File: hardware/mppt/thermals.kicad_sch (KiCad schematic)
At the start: 6 parts, among them M401 Fan

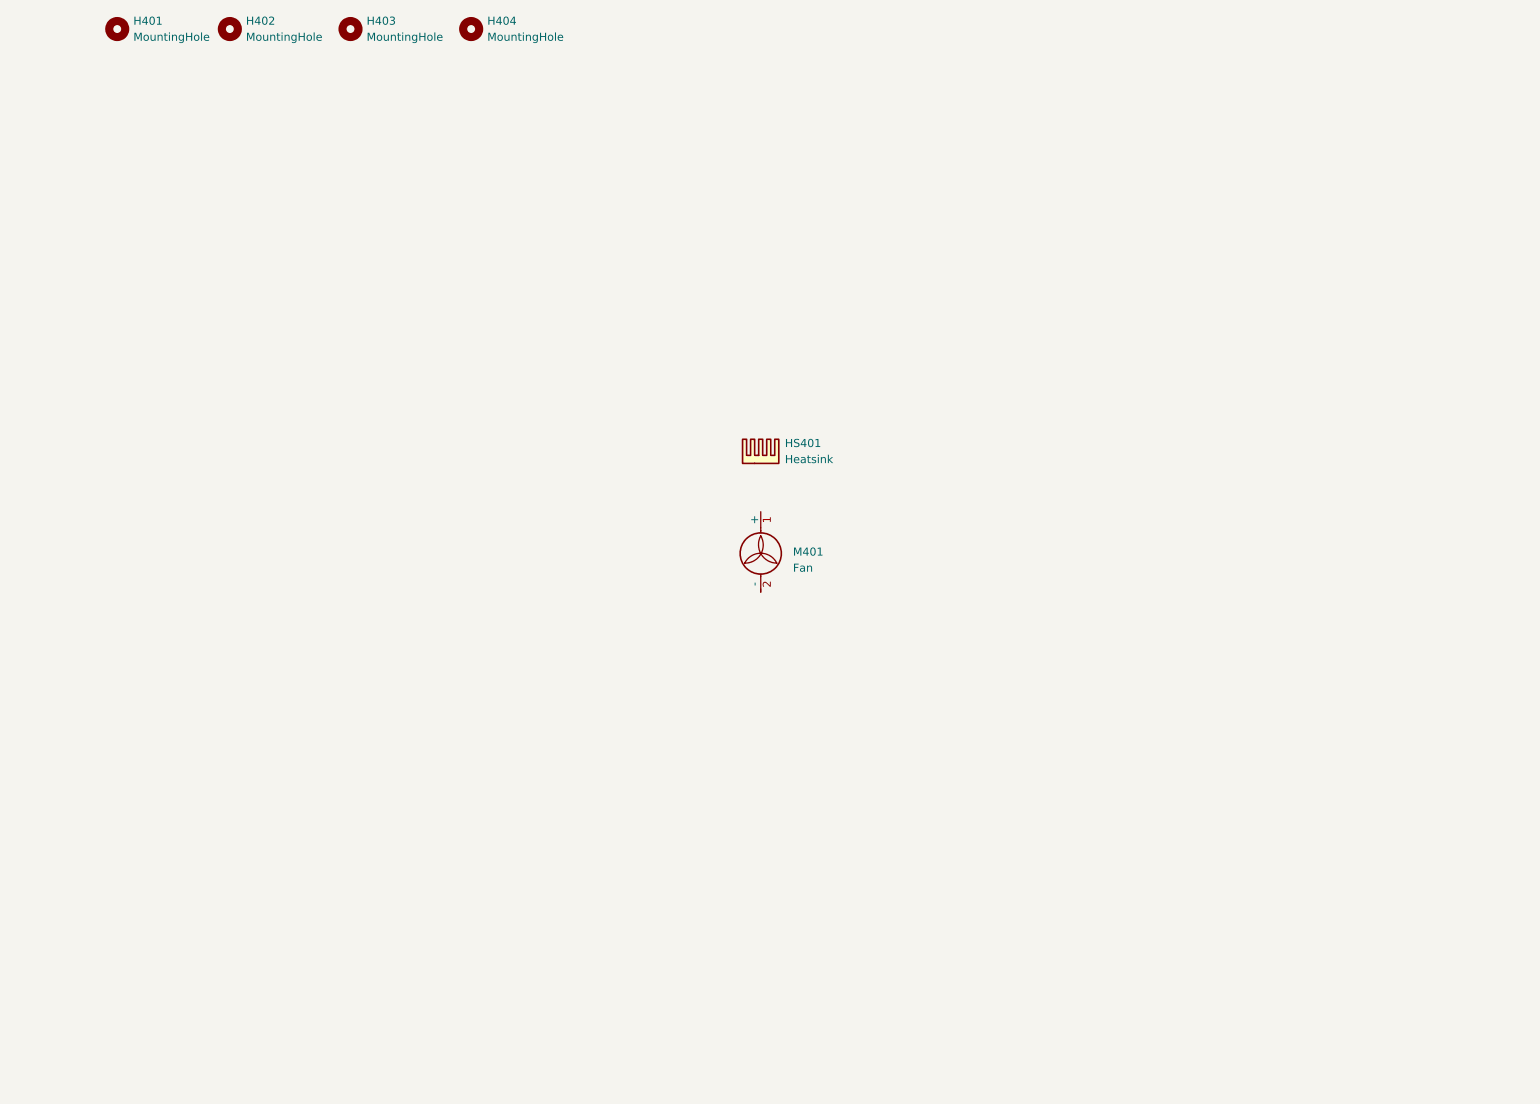
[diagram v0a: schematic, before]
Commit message: run through mppt sch, going through bom
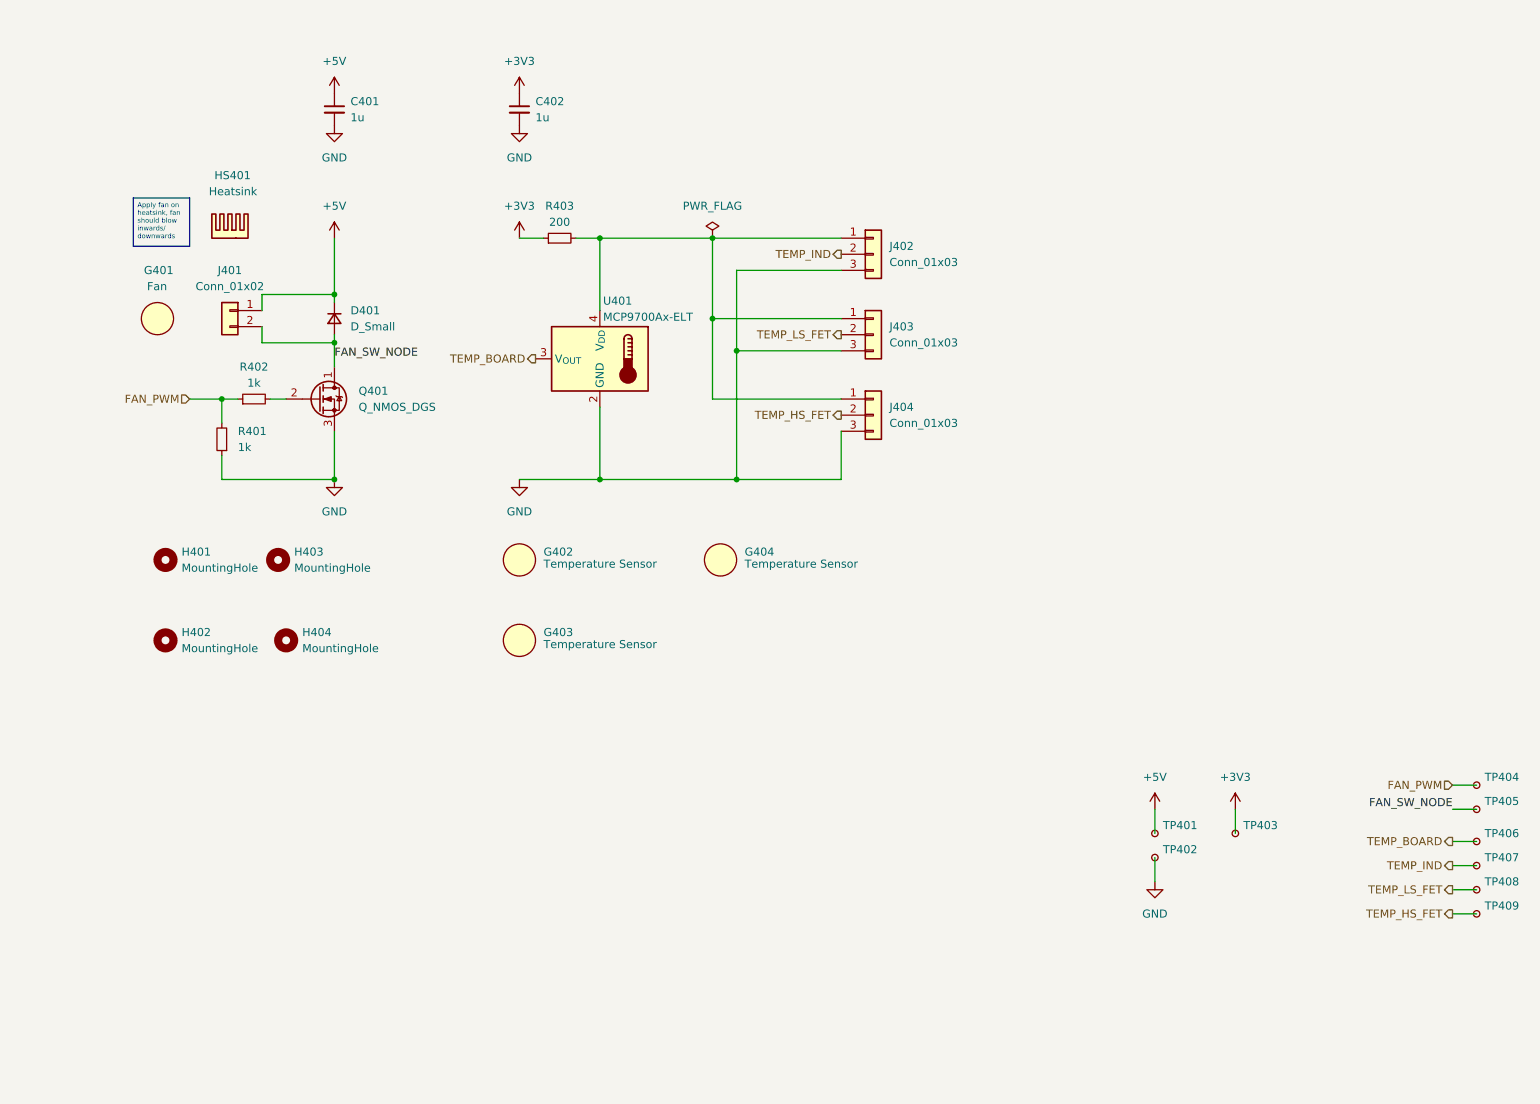
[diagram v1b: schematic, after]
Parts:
- removed M401: Fan, symbol Motor:Fan
- added C401, C402: 1u, symbol Device:C_Small
- added D401: D_Small, symbol Device:D_Small
- added G401: Fan, symbol generic_symbol:Generic_Symbol
- added G402, G403, G404: Temperature Sensor, symbol generic_symbol:Generic_Symbol
- added J401: Conn_01x02, symbol Connector_Generic:Conn_01x02
- added J402, J403, J404: Conn_01x03, symbol Connector_Generic:Conn_01x03
- added Q401: Q_NMOS_DGS, symbol Device:Q_NMOS_DGS
- added R401, R402: 1k, symbol Device:R_Small
- added R403: 200, symbol Device:R_Small
- added TP401, TP402, TP403, TP404, TP405, TP406, TP407, TP408, TP409: TestPoint_Small, TestPoint:TestPoint_Pad_D1.0mm, symbol Connector:TestPoint_Small
- added U401: MCP9700Ax-ELT, Package_TO_SOT_SMD:SOT-353_SC-70-5, symbol Sensor_Temperature:MCP9700Ax-ELT
- H401, H404: footprint MountingHole:MountingHole_5.3mm_M5 -> MountingHole:MountingHole_2.7mm_M2.5; Notes (none) -> M2.5 Hole
- H402: renamed from H403; footprint MountingHole:MountingHole_5.3mm_M5 -> MountingHole:MountingHole_2.7mm_M2.5; Notes (none) -> M2.5 Hole
- H403: renamed from H402; footprint MountingHole:MountingHole_5.3mm_M5 -> MountingHole:MountingHole_2.7mm_M2.5; Notes (none) -> M2.5 Hole
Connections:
- new net: J402.1 (Pin_1), J403.1 (Pin_1), J404.1 (Pin_1), R403.2, U401.4 (V_{DD})
- new net: Q401.2 (G), R402.2
- new net +3V3: C402.1, R403.1, TP403.1
- new net +5V: C401.1, D401.1 (K), J401.1 (Pin_1), TP401.1
- new net FAN_PWM: R401.2, R402.1, TP404.1
- new net FAN_SW_NODE: D401.2 (A), J401.2 (Pin_2), Q401.1 (D), TP405.1
- new net GND: C401.2, C402.2, J402.3 (Pin_3), J403.3 (Pin_3), J404.3 (Pin_3), Q401.3 (S), R401.1, TP402.1, U401.2 (GND)
- new net TEMP_BOARD: TP406.1, U401.3 (V_{OUT})
- new net TEMP_HS_FET: J404.2 (Pin_2), TP409.1
- new net TEMP_IND: J402.2 (Pin_2), TP407.1
- new net TEMP_LS_FET: J403.2 (Pin_2), TP408.1
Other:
- title: Mighty MPPT -> Thermals
- moved on the sheet: H401, H402, H403, H404, HS401

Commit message: update final missing pieces for sch, moving to bom pop
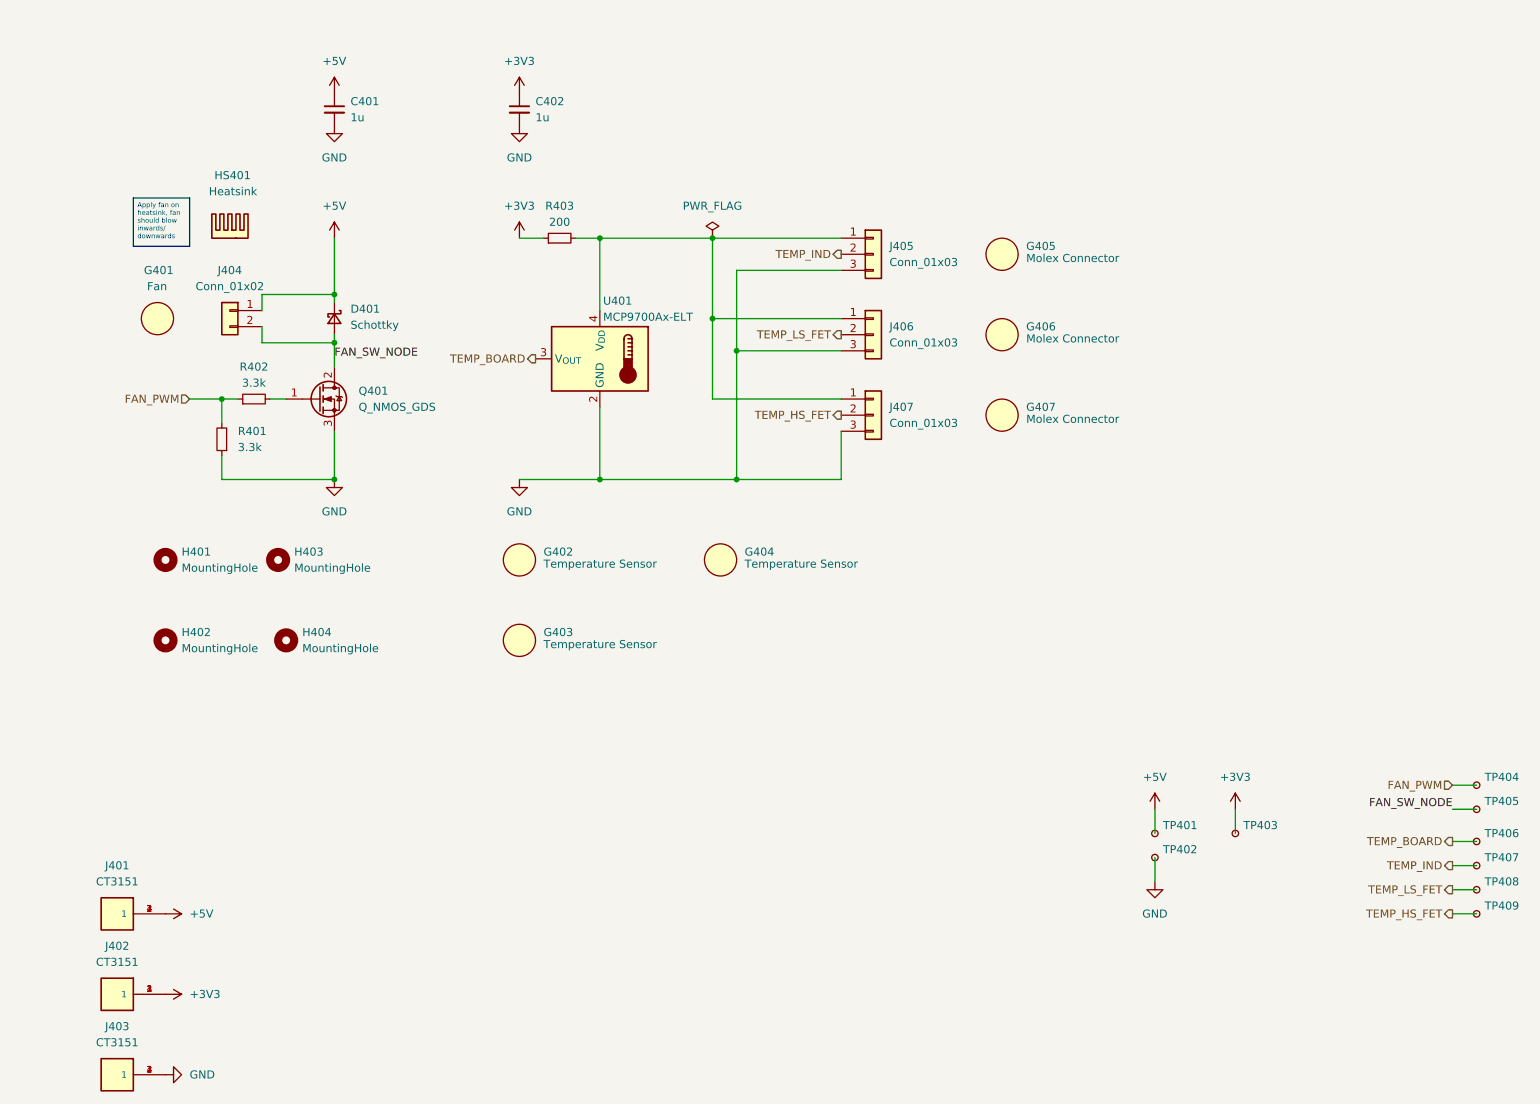
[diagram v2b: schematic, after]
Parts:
- removed J403, J404: Conn_01x03, symbol Connector_Generic:Conn_01x03
- removed Q401: Q_NMOS_DGS, symbol Device:Q_NMOS_DGS
- added G405, G406, G407: Molex Connector, symbol generic_symbol:Generic_Symbol
- added J401, J402, J403: CT3151, footprints:caltest_ct3151, symbol caltest_ct3151:CT3151
- added J406, J407: Conn_01x03, Connector_Molex:Molex_Micro-Fit_3.0_43650-0315_1x03_P3.00mm_Vertical, symbol Connector_Generic:Conn_01x03
- added Q401: Q_NMOS_GDS, Package_TO_SOT_SMD:SOT-223-3_TabPin2, symbol Device:Q_NMOS_GDS
- D401: value D_Small -> Schottky; symbol Device:D_Small -> Device:D_Schottky_Small; Notes (none) -> 0.55 Forward
- J404: renamed from J401; footprint (none) -> Connector_Molex:Molex_Micro-Fit_3.0_43650-0215_1x02_P3.00mm_Vertical
- J405: renamed from J402; footprint (none) -> Connector_Molex:Molex_Micro-Fit_3.0_43650-0315_1x03_P3.00mm_Vertical; Manufacturer (none) -> Molex; P/N (none) -> 43650-0315
- R401, R402: value 1k -> 3.3k; Manufacturer (none) -> Vishay / Dale
- R403: Manufacturer (none) -> Vishay / Dale
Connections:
- net +3V3: now also J402.1, J402.2 (1), J402.3 (1), J402.4 (1)
- net +5V: now also J401.1, J401.2 (1), J401.3 (1), J401.4 (1)
- net FAN_SW_NODE: now also Q401.2 (D)
- net GND: now also J403.1, J403.2 (1), J403.3 (1), J403.4 (1), J406.3 (Pin_3), J407.3 (Pin_3), Q401.3 (S)
- net TEMP_HS_FET: now also J407.2 (Pin_2)
- net TEMP_LS_FET: now also J406.2 (Pin_2)
- net at J405.1 (Pin_1), R403.2, U401.4 (V_{DD}): now also J406.1 (Pin_1), J407.1 (Pin_1)
- net at R402.2: now also Q401.1 (G)

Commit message: bom consolidated, starting layout
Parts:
- removed J401, J402, J403: CT3151, footprints:caltest_ct3151, symbol caltest_ct3151:CT3151
- removed TP401, TP402, TP403: TestPoint_Small, TestPoint:TestPoint_Pad_D1.0mm, symbol Connector:TestPoint_Small
- added G402: Molex Connector, symbol generic_symbol:Generic_Symbol
- added G403: Thermal Interface Pad, symbol generic_symbol:Generic_Symbol
- added TP401, TP402, TP403: TestPoint, TestPoint:TestPoint_Keystone_5000-5004_Miniature, symbol Connector:TestPoint
- C401, C402: footprint (none) -> Capacitor_SMD:C_0603_1608Metric_Pad1.08x0.95mm_HandSolder; Manufacturer Samsung Electro-Mechanics -> TDK; P/N (none) -> CGA3E1X7R1V105K080AC
- D401: footprint (none) -> Diode_SMD:D_SOD-123F; Manufacturer (none) -> Diodes Incorporated; Notes 0.55 Forward -> (none); P/N (none) -> SBR3U40S1F-7
- HS401: Manufacturer (none) -> Wakefield Thermal; P/N (none) -> 624-60AB
- J401: renamed from J404; Manufacturer (none) -> Molex; P/N (none) -> 43650-0215
- R401, R402: footprint (none) -> Resistor_SMD:R_0603_1608Metric_Pad0.98x0.95mm_HandSolder; P/N (none) -> CRCW06033K30FKEA
- R403: value 200 -> 205; footprint (none) -> Resistor_SMD:R_0603_1608Metric_Pad0.98x0.95mm_HandSolder; P/N (none) -> CRCW0603205RFKEA
- renumbered G402 to G404, G403 to G405, G404 to G406, G405 to G407, G406 to G408, G407 to G409, J405 to J402, J406 to J403, J407 to J404
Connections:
- net +3V3: now also TP403.1
- net +5V: now also TP401.1
- net GND: now also TP402.1
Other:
- moved on the sheet: G401
